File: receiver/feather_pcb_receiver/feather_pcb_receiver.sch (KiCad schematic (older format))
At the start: 21 parts

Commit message: removed eagle version and added connectors to kciad version
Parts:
- removed U?: nRF24L01P, Package_DFN_QFN:QFN-20-1EP_4x4mm_P0.5mm_EP2.5x2.5mm, symbol RF:nRF24L01P
- added U3: nRF24L01+, mysensors_radios:NRF24L01_PA_LNA-SMD, symbol nRF24L01+:nRF24L01+
- J2, J3: renamed from J?; footprint (none) -> crf1:MICRO_JST_6
- gave numbers to parts that had none: 18
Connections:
- net +3V3: now also U3.2 (VCC)
- net +5V: now also U3.1 (GND)
- net CE: now also U3.3 (CE)
- net CSN: now also U3.4 (CSN)
- net MISO: now also U3.7 (MISO)
- net MOSI: now also U3.6 (MOSI)
- net SCK: now also U3.5 (SCK)
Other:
- note added: "Todo: Connect those two\n"
- note added: "check pin numbers with footprint\ndo we need IRQ?"
- note removed: "This is the IC Version, we need the module version\n"

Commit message: added additional footprints and continued to layout
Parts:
- C3, C4, C7, C8: footprint (none) -> Capacitor_SMD:C_0805_2012Metric
- D1: footprint (none) -> LED_SMD:LED_0805_2012Metric
- J2: footprint crf1:MICRO_JST_6 -> Connector_PinHeader_2.00mm:PinHeader_1x04_P2.00mm_Vertical
- J4: footprint (none) -> crf1:MICRO_JST_6
- R1, R2: footprint (none) -> Resistor_SMD:R_0805_2012Metric
- Y1: footprint (none) -> Crystal:Crystal_SMD_2012-2Pin_2.0x1.2mm
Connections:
- net +5V: no longer C1.2, C2.2, C3.1, C4.2, C5.2, C6.2, C7.2, C8.2, J1.5 (GND), J1.6 (Shield), J2.4 (Pin_4), MOD1.1 (GND), MOD1.10 (GND), MOD1.8 (GND), R2.2, U1.2 (GND), U2.18 (GND), U2.35 (GND), U2.42 (GND), U3.1 (GND)
- new net GND: C1.2, C2.2, C3.1, C4.2, C5.2, C6.2, C7.2, C8.2, J1.5 (GND), J1.6 (Shield), J2.4 (Pin_4), MOD1.1 (GND), MOD1.10 (GND), MOD1.8 (GND), R2.2, U1.2 (GND), U2.18 (GND), U2.35 (GND), U2.42 (GND), U3.1 (GND)
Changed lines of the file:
@@
 F 0 "D1" H 4893 4416 50  0000 C CNN
 F 1 "LED" H 4893 4325 50  0000 C CNN
-F 2 "" H 4900 4200 50  0001 C CNN
+F 2 "LED_SMD:LED_0805_2012Metric" H 4900 4200 50  0001 C CNN
 F 3 "~" H 4900 4200 50  0001 C CNN
 	1    4900 4200
@@
 F 0 "Y1" V 4950 2400 50  0000 R CNN
 F 1 "ABS06-127-32.768KHZ-T‎" V 5000 2600 20  0000 R CNN
-F 2 "" H 4800 2450 50  0001 C CNN
+F 2 "Crystal:Crystal_SMD_2012-2Pin_2.0x1.2mm" H 4800 2450 50  0001 C CNN
 F 3 "~" H 4800 2450 50  0001 C CNN
 	1    4800 2450
@@
 F 0 "J4" H 8372 3174 50  0000 R CNN
 F 1 "Utilities Conn" H 8372 3083 50  0000 R CNN
-F 2 "" H 8400 3200 50  0001 C CNN
+F 2 "crf1:MICRO_JST_6" H 8400 3200 50  0001 C CNN
 F 3 "~" H 8400 3200 50  0001 C CNN
 	1    8400 3200
@@
 F 0 "J2" H 8372 1724 50  0000 R CNN
 F 1 "uC_Flash" H 8372 1633 50  0000 R CNN
-F 2 "crf1:MICRO_JST_6" H 8400 1750 50  0001 C CNN
+F 2 "Connector_PinHeader_2.00mm:PinHeader_1x04_P2.00mm_Vertical" H 8400 1750 50  0001 C CNN
 F 3 "~" H 8400 1750 50  0001 C CNN
 	1    8400 1750
@@
 	8200 1850 7900 1850
 $Comp
-L Device:C_Small C3
-U 1 1 5CD6ACAC
-P 2150 1700
-F 0 "C3" H 2100 1900 50  0000 L CNN
-F 1 "0.1uF" H 2050 2000 50  0000 L CNN
-F 2 "" H 2150 1700 50  0001 C CNN
-F 3 "~" H 2150 1700 50  0001 C CNN
-	1    2150 1700
-	1    0    0    -1
-$EndComp
-$Comp
 L Device:C_Small C2
 U 1 1 5CD6C170
@@
 Connection ~ 1850 1600
 Wire Wire Line
-	1850 1600 2150 1600
-Wire Wire Line
 	1550 1800 1850 1800
 Connection ~ 1850 1800
-Wire Wire Line
-	1850 1800 2150 1800
 $Comp
 L power:GND #PWR0104
@@
 F 0 "R1" H 2509 1796 50  0000 L CNN
 F 1 "100k" H 2509 1705 50  0000 L CNN
-F 2 "" H 2450 1750 50  0001 C CNN
+F 2 "Resistor_SMD:R_0805_2012Metric" H 2450 1750 50  0001 C CNN
 F 3 "~" H 2450 1750 50  0001 C CNN
 	1    2450 1750
@@
 Wire Wire Line
 	2450 1600 2450 1650
-Wire Wire Line
-	2450 1600 2150 1600
 Connection ~ 2450 1600
-Connection ~ 2150 1600
 $Comp
 L Device:C_Small C4
@@
 F 0 "C4" H 3650 1900 50  0000 L CNN
 F 1 "0.1uF" H 3600 2000 50  0000 L CNN
-F 2 "" H 3700 1700 50  0001 C CNN
+F 2 "Capacitor_SMD:C_0805_2012Metric" H 3700 1700 50  0001 C CNN
 F 3 "~" H 3700 1700 50  0001 C CNN
 	1    3700 1700
@@
 F 0 "R2" V 4304 4200 50  0000 C CNN
 F 1 "1K" V 4395 4200 50  0000 C CNN
-F 2 "" H 4500 4200 50  0001 C CNN
+F 2 "Resistor_SMD:R_0805_2012Metric" H 4500 4200 50  0001 C CNN
 F 3 "~" H 4500 4200 50  0001 C CNN
 	1    4500 4200
@@
 F 0 "C8" V 4300 2550 50  0000 L CNN
 F 1 "0.1uF" V 4600 2500 50  0000 L CNN
-F 2 "" H 4450 2600 50  0001 C CNN
+F 2 "Capacitor_SMD:C_0805_2012Metric" H 4450 2600 50  0001 C CNN
 F 3 "~" H 4450 2600 50  0001 C CNN
 	1    4450 2600
@@
 F 0 "C7" V 4300 2150 50  0000 L CNN
 F 1 "0.1uF" V 4600 2100 50  0000 L CNN
-F 2 "" H 4450 2200 50  0001 C CNN
+F 2 "Capacitor_SMD:C_0805_2012Metric" H 4450 2200 50  0001 C CNN
 F 3 "~" H 4450 2200 50  0001 C CNN
 	1    4450 2200
@@
 Wire Wire Line
 	4800 2200 5150 2200
-Wire Wire Line
-	8000 1950 8000 2100
-Wire Wire Line
-	7700 2100 8000 2100
-Connection ~ 8000 2100
-Wire Wire Line
-	8000 2100 8000 3600
 Text GLabel 8300 5550 0    50   Input ~ 0
 CSN
@@
 Text Notes 8300 2800 0    50   ~ 0
 Todo: Connect those two\n
+Wire Wire Line
+	1850 1600 2150 1600
+$Comp
+L Device:C_Small C3
+U 1 1 5CD6ACAC
+P 2150 1700
+F 0 "C3" H 2100 1900 50  0000 L CNN
+F 1 "0.1uF" H 2050 2000 50  0000 L CNN
+F 2 "Capacitor_SMD:C_0805_2012Metric" H 2150 1700 50  0001 C CNN
+F 3 "~" H 2150 1700 50  0001 C CNN
+	1    2150 1700
+	1    0    0    1
+$EndComp
+Connection ~ 2150 1600
+Wire Wire Line
+	2150 1600 2450 1600
+Wire Wire Line
+	1850 1800 2150 1800
+Wire Wire Line
+	8000 1950 8000 3600
 $EndSCHEMATC

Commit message: rfm module layout
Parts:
- removed AE1: Antenna, symbol Device:Antenna
- added AE1: Antenna_Shield, Connector_Coaxial:U.FL_Hirose_U.FL-R-SMT-1_Vertical, symbol Device:Antenna_Shield
- C1, C2, C5, C6: footprint (none) -> Capacitor_SMD:C_1206_3216Metric
- J1: footprint (none) -> Connector_USB:USB_Micro-B_Molex-105017-0001
- U3: footprint mysensors_radios:NRF24L01_PA_LNA-SMD -> (none)
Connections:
- net +3V3: now also J3.1 (Pin_1), J4.1 (Pin_1)
- net GND: now also J3.2 (Pin_2), J4.2 (Pin_2), AE1.2 (Shield)
- net UT3: now reaches U2.12 (PA07)
- net UT3: now also J4.5 (Pin_5)
- net VESC2: now reaches U2.15 (PA10)
- net VESC2: now also J3.4 (Pin_4)
- net VESC1: now reaches U2.16 (PA11)
- net VESC1: now also J3.3 (Pin_3)
- net UT4: now reaches U2.24 (PA15)
- net UT4: now also J4.6 (Pin_6)
- net UT1: now reaches U2.25 (PA16)
- net UT1: now also J4.3 (Pin_3)
- net VESC3: now reaches U2.27 (PA18)
- net VESC3: now also J3.5 (Pin_5), J3.6 (Pin_6)
- net UT2: now reaches U2.28 (PA19)
- net UT2: now also J4.4 (Pin_4)
- net at MOD1.9 (ANT): now also AE1.1 (A)
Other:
- note removed: "GND?\n"
- note removed: "Todo: Connect those two\n"
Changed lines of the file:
@@
 F 0 "J1" V 5911 1130 50  0000 L CNN
 F 1 "USB_B_Micro" V 6002 1130 50  0000 L CNN
-F 2 "" H 6050 750 50  0001 C CNN
+F 2 "Connector_USB:USB_Micro-B_Molex-105017-0001" H 6050 750 50  0001 C CNN
 F 3 "~" H 6050 750 50  0001 C CNN
 	1    5900 800
@@
 	0    -1   -1   0
 $EndComp
-Wire Wire Line
-	8200 1850 7900 1850
 $Comp
 L Device:C_Small C2
@@
 F 0 "C2" H 1800 1900 50  0000 L CNN
 F 1 "10uF" H 1750 2000 50  0000 L CNN
-F 2 "" H 1850 1700 50  0001 C CNN
+F 2 "Capacitor_SMD:C_1206_3216Metric" H 1850 1700 50  0001 C CNN
 F 3 "~" H 1850 1700 50  0001 C CNN
 	1    1850 1700
@@
 F 0 "C1" H 1500 1900 50  0000 L CNN
 F 1 "CP_Small" H 1400 1550 50  0000 L CNN
-F 2 "" H 1550 1700 50  0001 C CNN
+F 2 "Capacitor_SMD:C_1206_3216Metric" H 1550 1700 50  0001 C CNN
 F 3 "~" H 1550 1700 50  0001 C CNN
 	1    1550 1700
@@
 F 0 "C5" H 3900 1900 50  0000 L CNN
 F 1 "10uF" H 3850 2000 50  0000 L CNN
-F 2 "" H 3950 1700 50  0001 C CNN
+F 2 "Capacitor_SMD:C_1206_3216Metric" H 3950 1700 50  0001 C CNN
 F 3 "~" H 3950 1700 50  0001 C CNN
 	1    3950 1700
@@
 F 0 "C6" H 4250 1800 50  0000 L CNN
 F 1 "CP_Small" H 4050 1550 50  0000 L CNN
-F 2 "" H 4200 1700 50  0001 C CNN
+F 2 "Capacitor_SMD:C_1206_3216Metric" H 4200 1700 50  0001 C CNN
 F 3 "~" H 4200 1700 50  0001 C CNN
 	1    4200 1700
@@
 Wire Wire Line
 	6100 1150 6100 1100
-$Comp
-L power:+5V #PWR0111
-U 1 1 5CD8362A
-P 7700 2100
-F 0 "#PWR0111" H 7700 1950 50  0001 C CNN
-F 1 "+5V" V 7715 2228 50  0000 L CNN
-F 2 "" H 7700 2100 50  0001 C CNN
-F 3 "" H 7700 2100 50  0001 C CNN
-	1    7700 2100
-	0    -1   -1   0
-$EndComp
 Wire Wire Line
 	5250 4200 5050 4200
@@
 	0    1    1    0
 $EndComp
-$Comp
-L Device:Antenna AE1
-U 1 1 5CDF4696
-P 1500 4050
-F 0 "AE1" V 1717 3993 50  0000 C CNN
-F 1 "Antenna" V 1626 3993 50  0000 C CNN
-F 2 "" H 1500 4050 50  0001 C CNN
-F 3 "~" H 1500 4050 50  0001 C CNN
-	1    1500 4050
-	0    -1   -1   0
-$EndComp
-Wire Wire Line
-	1700 4050 2050 4050
-Text Notes 1450 4200 0    50   ~ 0
-GND?\n
 Text Notes 8550 4650 0    50   ~ 0
 check pin numbers with footprint\ndo we need IRQ?
@@
 F 0 "U3" H 9250 5815 50  0000 C CNN
 F 1 "nRF24L01+" H 9250 5724 50  0000 C CNN
-F 2 "mysensors_radios:NRF24L01_PA_LNA-SMD" H 9250 5400 50  0001 C CNN
+F 2 "" H 9250 5400 50  0001 C CNN
 F 3 "" H 9250 5250 50  0001 C CNN
 	1    9250 5300
@@
 Wire Wire Line
 	10300 5400 10000 5400
-Text Notes 8300 2800 0    50   ~ 0
-Todo: Connect those two\n
 Wire Wire Line
 	1850 1600 2150 1600
@@
 	1850 1800 2150 1800
 Wire Wire Line
-	8000 1950 8000 3600
+	8000 1950 8000 2200
+Wire Wire Line
+	7900 1850 7950 1850
+Wire Wire Line
+	8200 2100 7950 2100
+Wire Wire Line
+	7950 2100 7950 1850
+Connection ~ 7950 1850
+Wire Wire Line
+	7950 1850 8200 1850
+Wire Wire Line
+	8200 2200 8000 2200
+Connection ~ 8000 2200
+Wire Wire Line
+	8000 2200 8000 3100
+Text GLabel 7750 2300 0    50   Input ~ 0
+VESC1
+Text GLabel 7750 2400 0    50   Input ~ 0
+VESC2
+Text GLabel 7750 2500 0    50   Input ~ 0
+VESC3
+Text GLabel 7750 2600 0    50   Input ~ 0
+VESC4
+Wire Wire Line
+	8200 2300 7750 2300
+Wire Wire Line
+	8200 2400 7750 2400
+Wire Wire Line
+	8200 2500 7850 2500
+Wire Wire Line
+	8200 2600 7850 2600
+Text GLabel 5050 3600 0    50   Input ~ 0
+VESC1
+Wire Wire Line
+	5050 3600 5250 3600
+Text GLabel 5050 3500 0    50   Input ~ 0
+VESC2
+Wire Wire Line
+	5050 3500 5250 3500
+Text GLabel 5150 4300 0    50   Input ~ 0
+VESC3
+Text GLabel 7750 3200 0    50   Input ~ 0
+UT1
+Text GLabel 7750 3300 0    50   Input ~ 0
+UT2
+Text GLabel 7750 3400 0    50   Input ~ 0
+UT3
+Text GLabel 7750 3500 0    50   Input ~ 0
+UT4
+Wire Wire Line
+	8000 3100 8200 3100
+Connection ~ 8000 3100
+Wire Wire Line
+	8000 3100 8000 3600
+Wire Wire Line
+	7950 2100 7950 3000
+Wire Wire Line
+	7950 3000 8200 3000
+Connection ~ 7950 2100
+Wire Wire Line
+	7750 3200 8200 3200
+Wire Wire Line
+	7750 3300 8200 3300
+Wire Wire Line
+	7750 3400 8200 3400
+Wire Wire Line
+	7750 3500 8200 3500
+Text GLabel 5150 4100 0    50   Input ~ 0
+UT1
+Wire Wire Line
+	5150 4100 5250 4100
+Text GLabel 5150 4400 0    50   Input ~ 0
+UT2
+Wire Wire Line
+	5150 4300 5250 4300
+Wire Wire Line
+	7850 2500 7850 2600
+Connection ~ 7850 2500
+Wire Wire Line
+	7850 2500 7750 2500
+Connection ~ 7850 2600
+Wire Wire Line
+	7850 2600 7750 2600
+Wire Wire Line
+	5150 4400 5250 4400
+Text GLabel 5050 3200 0    50   Input ~ 0
+UT3
+Wire Wire Line
+	5050 3200 5250 3200
+Text GLabel 5050 4000 0    50   Input ~ 0
+UT4
+Wire Wire Line
+	5050 4000 5250 4000
+$Comp
+L Device:Antenna_Shield AE1
+U 1 1 5CF58F9F
+P 1500 4050
+F 0 "AE1" V 1283 4043 50  0000 C CNN
+F 1 "Antenna_Shield" V 1374 4043 50  0000 C CNN
+F 2 "Connector_Coaxial:U.FL_Hirose_U.FL-R-SMT-1_Vertical" H 1500 4150 50  0001 C CNN
+F 3 "~" H 1500 4150 50  0001 C CNN
+	1    1500 4050
+	0    -1   1    0
+$EndComp
+Wire Wire Line
+	1700 4150 1900 4150
+Wire Wire Line
+	1900 4150 1900 4350
+Wire Wire Line
+	1900 4350 2450 4350
+Connection ~ 2450 4350
+Wire Wire Line
+	1700 4050 2050 4050
 $EndSCHEMATC

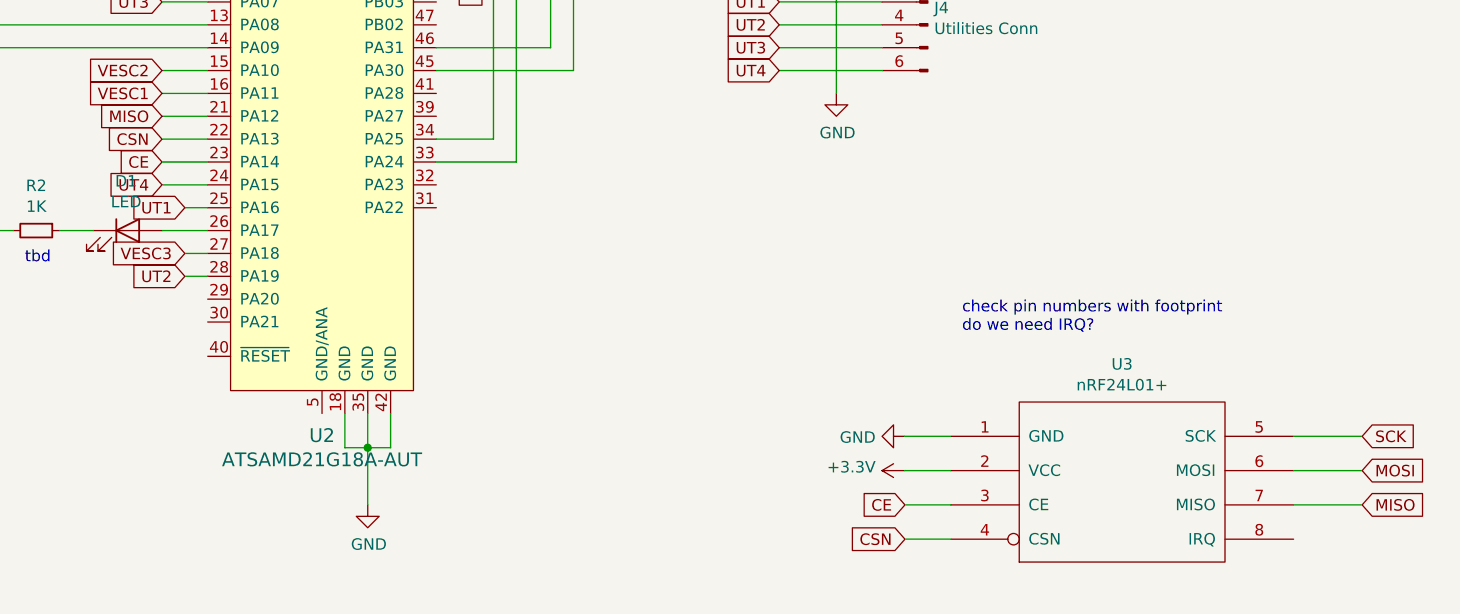
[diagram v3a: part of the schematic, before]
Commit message: added nrf module
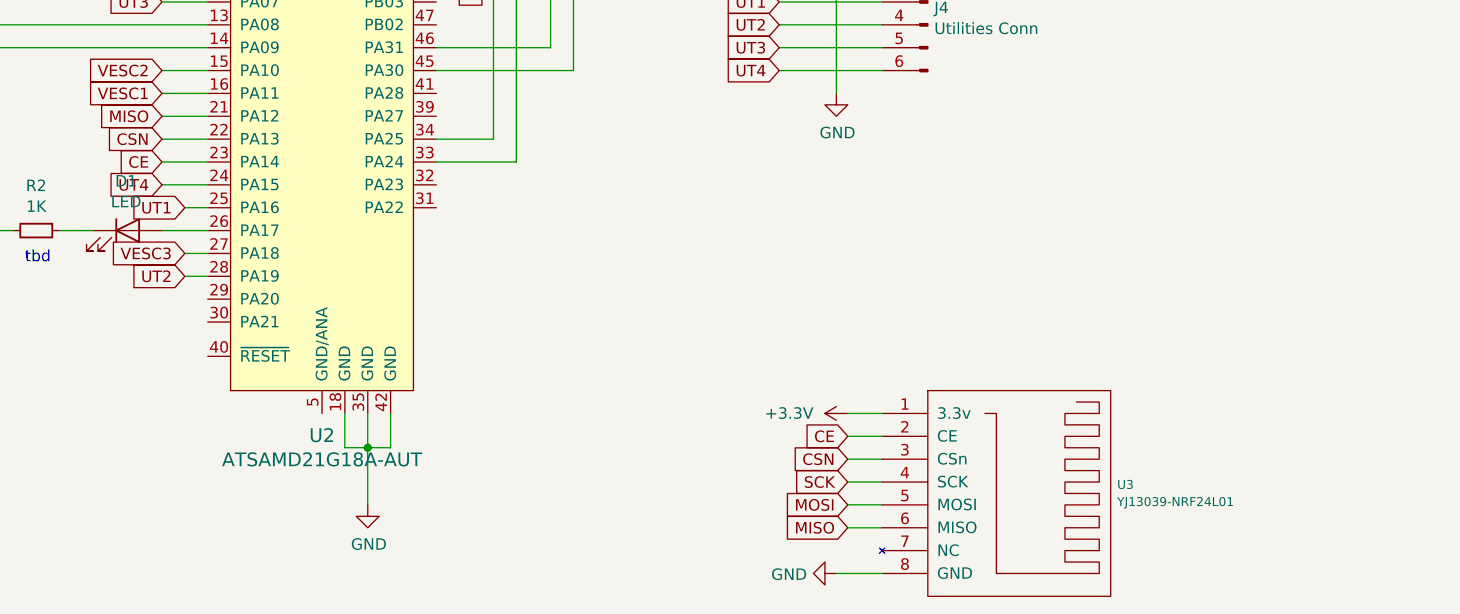
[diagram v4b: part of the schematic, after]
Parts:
- removed U3: nRF24L01+, symbol nRF24L01+:nRF24L01+
- added U3: YJ13039-NRF24L01, mysensors_radios:YJ-13039-NRF24L01, symbol yj13039-nrf24l01:YJ13039-NRF24L01
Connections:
- net +3V3: now also U3.1 (3.3v)
- net CE: now also U3.2 (CE)
- net CSN: now also U3.3 (CSn)
- net GND: now also U3.8 (GND)
- net MISO: now also U3.6 (MISO)
- net MOSI: now also U3.5 (MOSI)
- net SCK: now also U3.4 (SCK)
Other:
- note removed: "check pin numbers with footprint\ndo we need IRQ?"
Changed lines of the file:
@@
 Wire Wire Line
 	4050 3400 5250 3400
-Text GLabel 10300 5250 2    50   Input ~ 0
-MOSI
-Text GLabel 10300 5400 2    50   Input ~ 0
-MISO
-Text GLabel 10300 5100 2    50   Input ~ 0
-SCK
 Wire Wire Line
 	4800 2300 4800 2200
@@
 Wire Wire Line
 	4800 2200 5150 2200
-Text GLabel 8300 5550 0    50   Input ~ 0
-CSN
 Text GLabel 5050 3800 0    50   Input ~ 0
 CSN
-Wire Wire Line
-	5050 3800 5250 3800
-Text GLabel 8300 5400 0    50   Input ~ 0
-CE
 Text GLabel 5050 3900 0    50   Input ~ 0
 CE
-Wire Wire Line
-	5050 3900 5250 3900
-$Comp
-L power:+3.3V #PWR0117
-U 1 1 5CDDB188
-P 8300 5250
-F 0 "#PWR0117" H 8300 5100 50  0001 C CNN
-F 1 "+3.3V" V 8315 5378 50  0000 L CNN
-F 2 "" H 8300 5250 50  0001 C CNN
-F 3 "" H 8300 5250 50  0001 C CNN
-	1    8300 5250
-	0    -1   -1   0
-$EndComp
-$Comp
-L power:GND #PWR0118
-U 1 1 5CDDF200
-P 8300 5100
-F 0 "#PWR0118" H 8300 4850 50  0001 C CNN
-F 1 "GND" V 8305 4972 50  0000 R CNN
-F 2 "" H 8300 5100 50  0001 C CNN
-F 3 "" H 8300 5100 50  0001 C CNN
-	1    8300 5100
-	0    1    1    0
-$EndComp
-Text Notes 8550 4650 0    50   ~ 0
-check pin numbers with footprint\ndo we need IRQ?
-$Comp
-L nRF24L01+:nRF24L01+ U3
-U 1 1 5CD631F7
-P 9250 5300
-F 0 "U3" H 9250 5815 50  0000 C CNN
-F 1 "nRF24L01+" H 9250 5724 50  0000 C CNN
-F 2 "" H 9250 5400 50  0001 C CNN
-F 3 "" H 9250 5250 50  0001 C CNN
-	1    9250 5300
-	1    0    0    -1
-$EndComp
-Wire Wire Line
-	8300 5100 8500 5100
-Wire Wire Line
-	8300 5250 8500 5250
-Wire Wire Line
-	8300 5400 8500 5400
-Wire Wire Line
-	8300 5550 8500 5550
-Wire Wire Line
-	10000 5100 10300 5100
-Wire Wire Line
-	10300 5250 10000 5250
-Wire Wire Line
-	10300 5400 10000 5400
 Wire Wire Line
 	1850 1600 2150 1600
@@
 Wire Wire Line
 	1700 4050 2050 4050
+Wire Wire Line
+	8000 5700 8200 5700
+Wire Wire Line
+	8050 5500 8200 5500
+Wire Wire Line
+	8050 5400 8200 5400
+Wire Wire Line
+	8050 5300 8200 5300
+Wire Wire Line
+	8050 5200 8200 5200
+Wire Wire Line
+	8050 5100 8200 5100
+Wire Wire Line
+	8050 5000 8200 5000
+$Comp
+L yj13039-nrf24l01:YJ13039-NRF24L01 U3
+U 1 1 5D0851A7
+P 8400 4900
+F 0 "U3" V 8812 5728 39  0000 L CNN
+F 1 "YJ13039-NRF24L01" V 8887 5728 39  0000 L CNN
+F 2 "mysensors_radios:YJ-13039-NRF24L01" H 8400 4900 39  0001 C CNN
+F 3 "" H 8400 4900 39  0001 C CNN
+	1    8400 4900
+	0    1    1    0
+$EndComp
+$Comp
+L power:GND #PWR0118
+U 1 1 5CDDF200
+P 8000 5700
+F 0 "#PWR0118" H 8000 5450 50  0001 C CNN
+F 1 "GND" V 8005 5572 50  0000 R CNN
+F 2 "" H 8000 5700 50  0001 C CNN
+F 3 "" H 8000 5700 50  0001 C CNN
+	1    8000 5700
+	0    1    1    0
+$EndComp
+$Comp
+L power:+3.3V #PWR0117
+U 1 1 5CDDB188
+P 8050 5000
+F 0 "#PWR0117" H 8050 4850 50  0001 C CNN
+F 1 "+3.3V" V 8050 5150 50  0000 L CNN
+F 2 "" H 8050 5000 50  0001 C CNN
+F 3 "" H 8050 5000 50  0001 C CNN
+	1    8050 5000
+	0    -1   -1   0
+$EndComp
+Text GLabel 8050 5100 0    50   Input ~ 0
+CE
+Text GLabel 8050 5200 0    50   Input ~ 0
+CSN
+Text GLabel 8050 5300 0    50   Input ~ 0
+SCK
+Text GLabel 8050 5500 0    50   Input ~ 0
+MISO
+Text GLabel 8050 5400 0    50   Input ~ 0
+MOSI
+Wire Wire Line
+	5050 3800 5250 3800
+Wire Wire Line
+	5250 3900 5050 3900
 $EndSCHEMATC
